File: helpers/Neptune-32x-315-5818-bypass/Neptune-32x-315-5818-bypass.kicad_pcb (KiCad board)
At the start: 2 copper layers, 25.6 x 25.6 mm, 1 part, among them IC1 315-5818

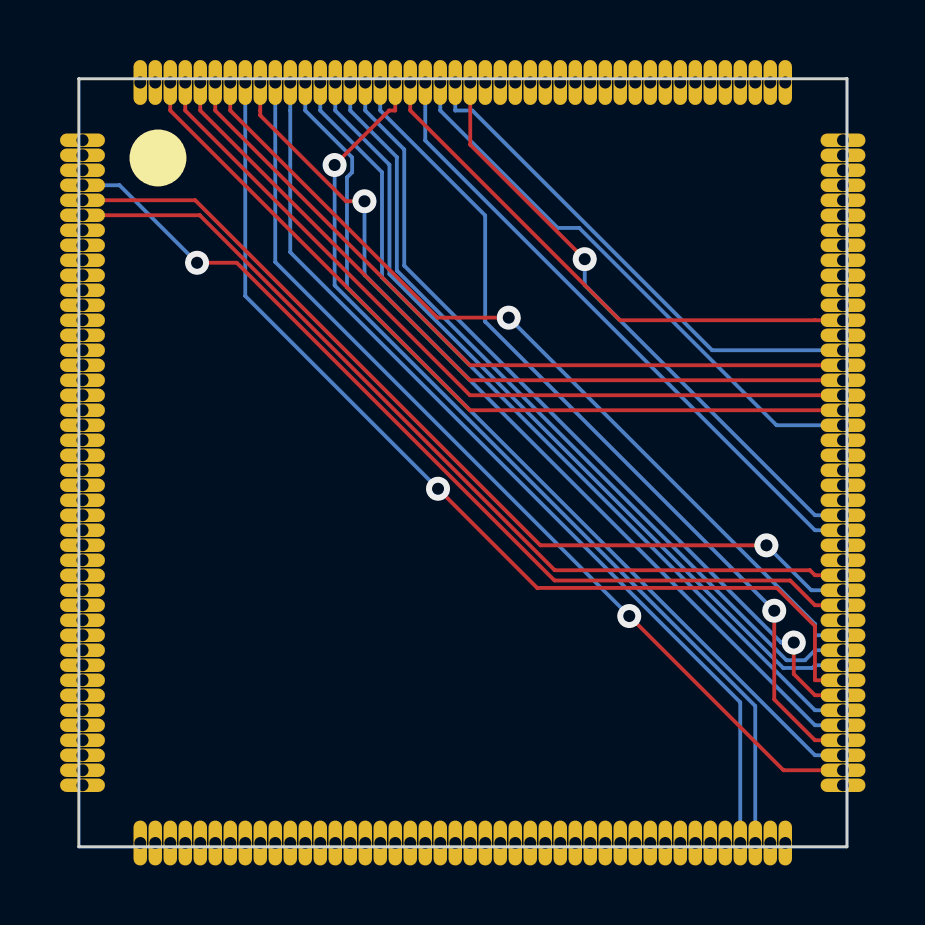
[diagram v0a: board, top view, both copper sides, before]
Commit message: Chnaged helper PCB's to be flex instead
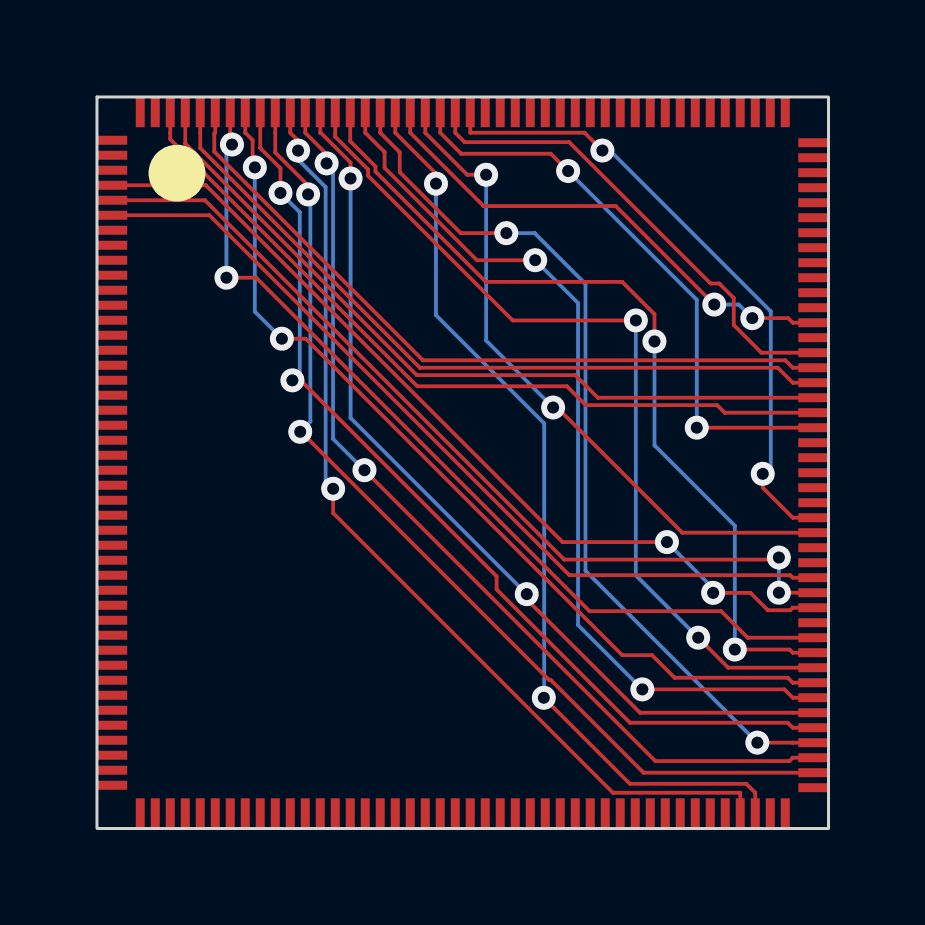
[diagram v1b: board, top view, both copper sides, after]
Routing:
- net VD10: track 33.4 -> 30.5 mm, vias 1 -> 2
- net VD2: track 27.8 -> 30.0 mm, vias 1 -> 2
- net VA21: track 30.3 -> 28.4 mm
- net VA19: track 31.1 -> 29.4 mm, vias 1 -> 2
- net VD9: track 30.4 -> 32.0 mm, vias 1 -> 2
- net VD5: track 28.7 -> 30.2 mm, vias 0 -> 2
- net ~{CLWR}: track 18.3 -> 16.7 mm, vias 0 -> 2
- net VD0: track 32.1 -> 30.6 mm, vias 1 -> 2
- net VD4: track 27.7 -> 29.2 mm, vias 0 -> 2
- net VD15: track 27.5 -> 26.1 mm
- net VD11: track 28.8 -> 30.1 mm, vias 1 -> 2
- net VD14: track 26.8 -> 25.5 mm
- net VD3: track 27.3 -> 28.5 mm, vias 0 -> 2
- net VD6: track 30.5 -> 31.8 mm, vias 0 -> 2
- net VD13: track 26.1 -> 24.9 mm
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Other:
- board size 25.6 x 25.6 mm -> 24.4 x 24.4 mm
